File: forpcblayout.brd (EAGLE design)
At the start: 110.5 x 63.7 mm, 76 parts, among them J1 3x2 M, J3 629105136821, SW2 !RESET, T1 2N2222, T2 2N2222, T3 2N2222, T4 2N2222, U3 ATMEGA32U4-AUR, X2 16 MHz

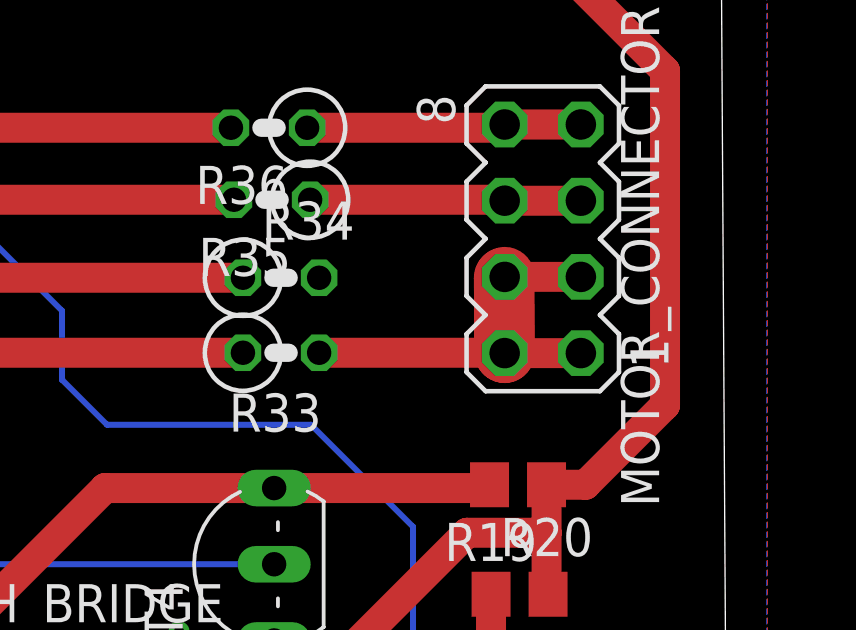
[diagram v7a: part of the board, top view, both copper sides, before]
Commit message: De-de-fucked motor header connections
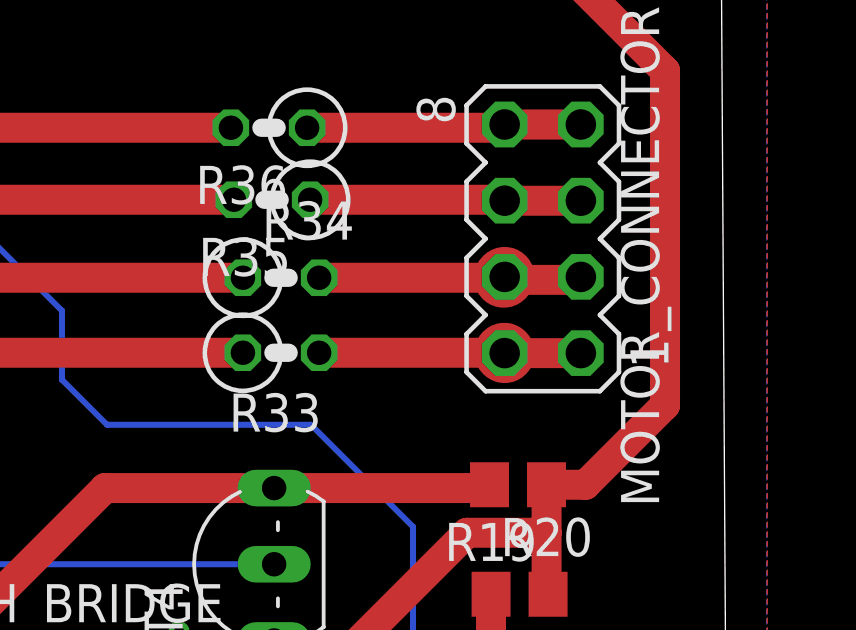
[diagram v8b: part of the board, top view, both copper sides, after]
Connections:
- net RIGHT_MOTOR1_0: now also MOTOR_CONNECTOR.1, MOTOR_CONNECTOR.2; no longer MOTOR_CONNECTOR.3, MOTOR_CONNECTOR.4
- net RIGHT_MOTOR2_0: now also MOTOR_CONNECTOR.3, MOTOR_CONNECTOR.4; no longer MOTOR_CONNECTOR.1, MOTOR_CONNECTOR.2
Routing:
- net RIGHT_MOTOR2_0: track 5.05 -> 8.82 mm
- net RIGHT_MOTOR1_0: track 11.2 -> 8.73 mm
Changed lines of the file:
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@@
 <contactref element="R33" pad="2"/>
 <wire x1="106.07" y1="25.5" x2="112.243209375" y2="25.5" width="1" layer="1"/>
-<wire x1="112.243209375" y1="25.5" x2="112.254678125" y2="28.02853125" width="2" layer="1"/>
-<wire x1="112.254678125" y1="28.02853125" x2="114.794678125" y2="28.02853125" width="1" layer="1"/>
-<contactref element="MOTOR_CONNECTOR" pad="4"/>
-<contactref element="MOTOR_CONNECTOR" pad="3"/>
+<wire x1="112.243209375" y1="25.5" x2="112.254678125" y2="25.48853125" width="2" layer="1"/>
+<wire x1="112.254678125" y1="25.48853125" x2="114.794678125" y2="25.48853125" width="1" layer="1"/>
+<contactref element="MOTOR_CONNECTOR" pad="2"/>
+<contactref element="MOTOR_CONNECTOR" pad="1"/>
 </signal>
 <signal name="PWM_3_0">
@@
 </signal>
 <signal name="RIGHT_MOTOR2_0">
-<wire x1="112.226146875" y1="28" x2="112.254678125" y2="25.48853125" width="2" layer="1"/>
-<wire x1="112.254678125" y1="25.48853125" x2="114.794678125" y2="25.48853125" width="1" layer="1"/>
-<contactref element="MOTOR_CONNECTOR" pad="2"/>
-<contactref element="MOTOR_CONNECTOR" pad="1"/>
+<wire x1="112.226146875" y1="28" x2="112.254678125" y2="28.02853125" width="2" layer="1"/>
+<wire x1="114.694678125" y1="27.92853125" x2="112.354678125" y2="27.92853125" width="1" layer="1"/>
+<wire x1="112.254678125" y1="28.02853125" x2="112.354678125" y2="27.92853125" width="1" layer="1"/>
+<wire x1="114.694678125" y1="27.92853125" x2="114.794678125" y2="28.02853125" width="1" layer="1"/>
+<contactref element="MOTOR_CONNECTOR" pad="4"/>
+<contactref element="MOTOR_CONNECTOR" pad="3"/>
 <contactref element="R34" pad="2"/>
-<wire x1="106.07" y1="28" x2="112.226146875" y2="28" width="0" layer="19" extent="1-1"/>
+<wire x1="106.07" y1="28" x2="112.226146875" y2="28" width="1" layer="1"/>
 </signal>
 <signal name="VBUS_0">
